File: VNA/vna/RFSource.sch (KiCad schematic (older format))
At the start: 0 parts

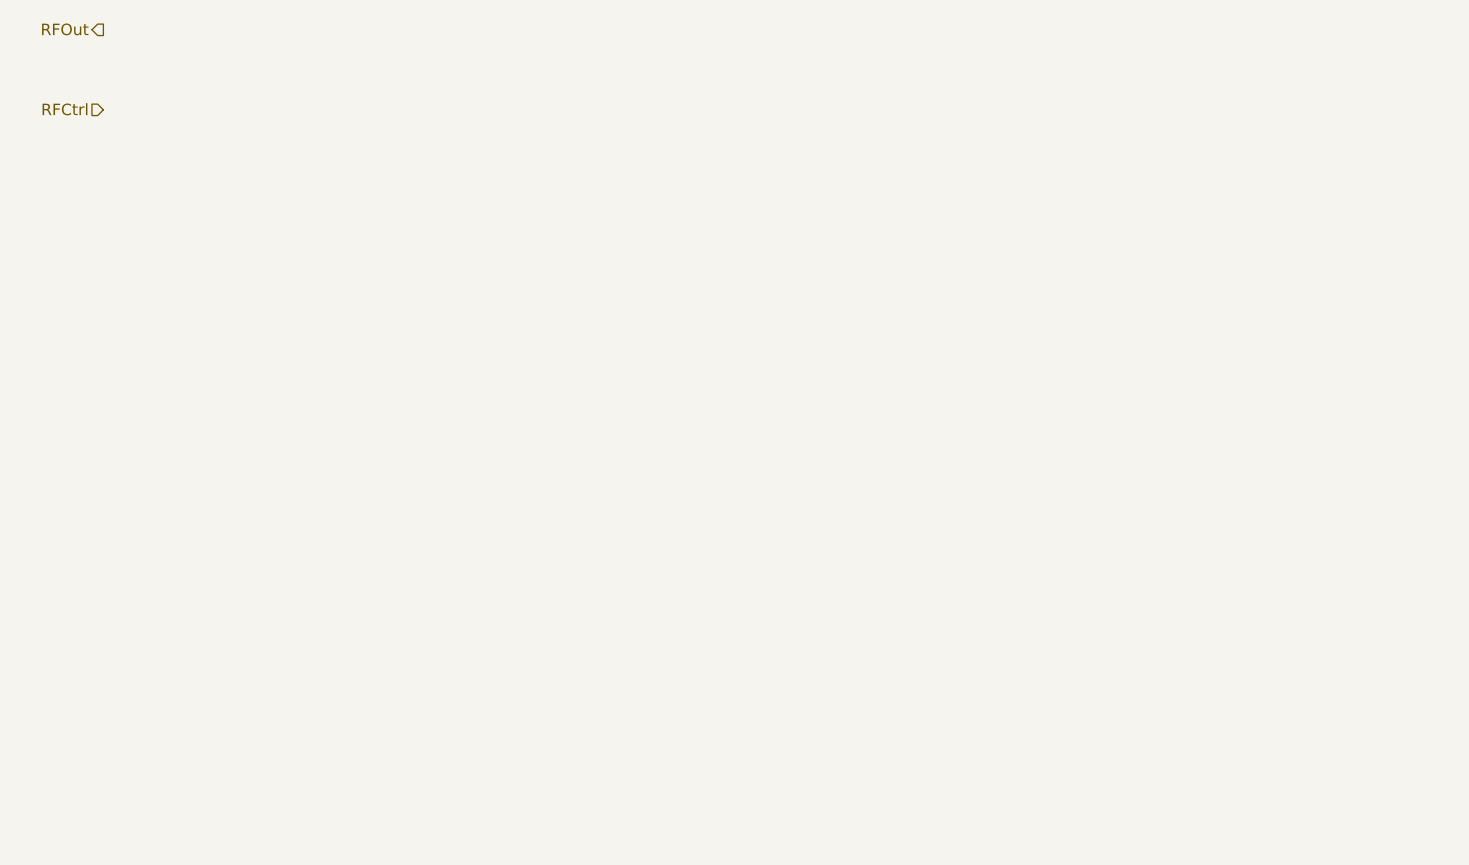
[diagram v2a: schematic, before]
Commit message: finished controller, chose compatible switches
controller and rf switches have been completed.

ToDo: finish filter design for RF Source, add auto gain control
ToDo: finish directional coupler footprints
ToDo: PCB Layout
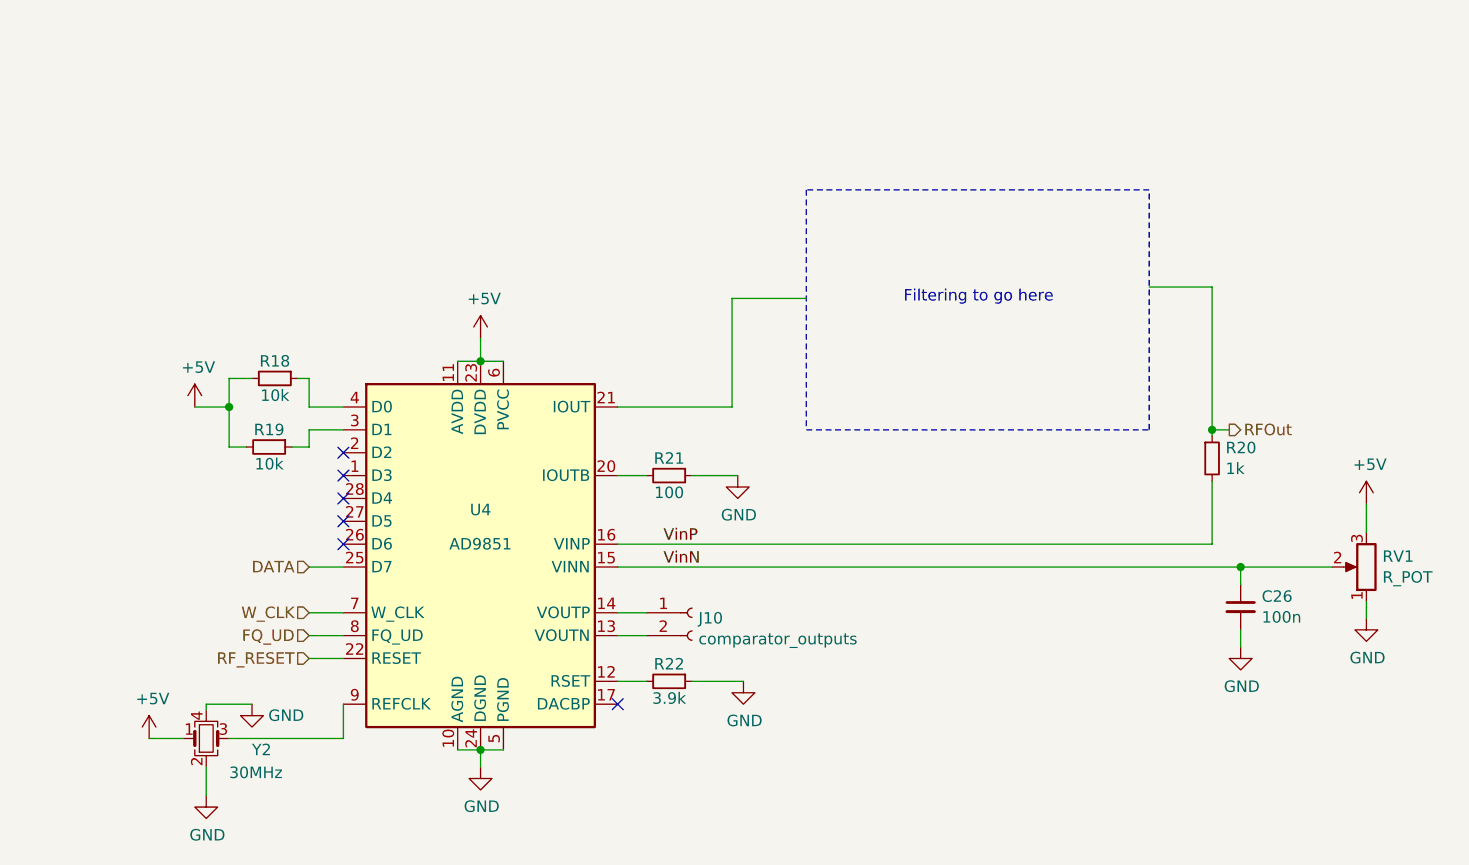
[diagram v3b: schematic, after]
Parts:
- added C26: 100n, symbol Device:C_Small
- added J10: comparator_outputs, symbol Connector:Conn_01x02_Female
- added R18, R19: 10k, symbol Device:R_Small
- added R20: 1k, symbol Device:R_Small
- added R21: 100, symbol Device:R_Small
- added R22: 3.9k, symbol Device:R_Small
- added RV1: R_POT, symbol Device:R_POT
- added U4: AD9851, Package_SO:SSOP-28_5.3x10.2mm_P0.65mm, symbol Interface:AD9851
- added Y2: 30MHz, symbol Device:Crystal_GND24_Small
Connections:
- net labels added: +5V, DATA, FQ_UD, GND, RF_RESET, VinN, VinP, W_CLK
- net labels removed: RFCtrl
- wire segments 0 -> 48
- no-connect marks 0 -> 6
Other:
- note added: "Filtering to go here"

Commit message: custom footprint for couplers, added decoupling caps
added custom footprint for directional couplers - will need to verify it

added decoupling caps to ad9851
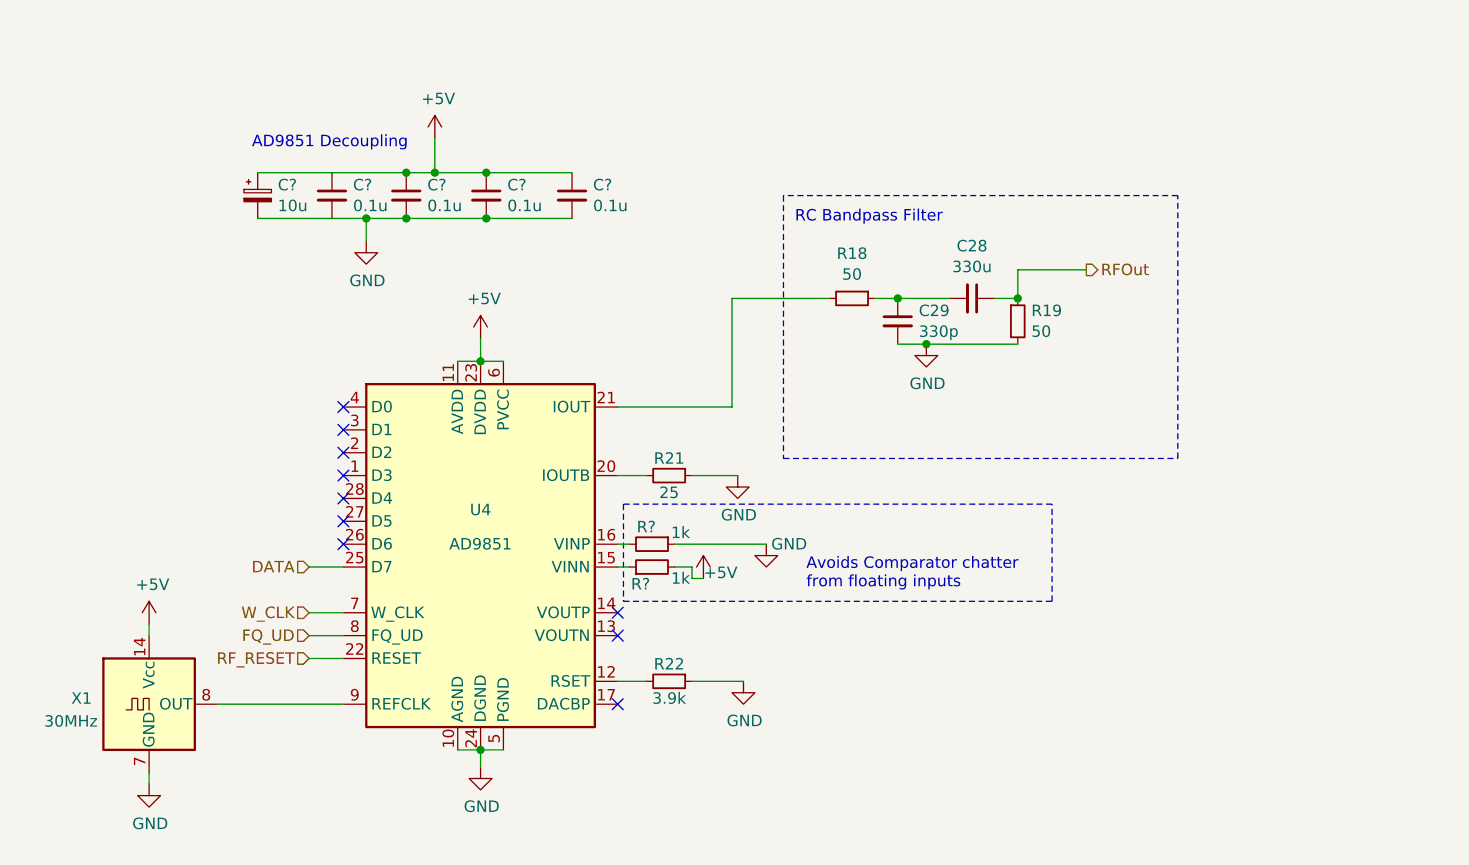
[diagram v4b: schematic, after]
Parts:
- removed C26: 100n, symbol Device:C_Small
- removed J10: comparator_outputs, symbol Connector:Conn_01x02_Female
- removed R20: 1k, symbol Device:R_Small
- removed RV1: R_POT, symbol Device:R_POT
- removed Y2: 30MHz, symbol Device:Crystal_GND24_Small
- added C28: 330u, Capacitor_SMD:C_1206_3216Metric_Pad1.42x1.75mm_HandSolder, symbol Device:C_Small
- added C29: 330p, Capacitor_SMD:C_1206_3216Metric_Pad1.42x1.75mm_HandSolder, symbol Device:C_Small
- added C? (x4): 0.1u, symbol Device:C_Small
- added C?: 10u, symbol Device:CP_Small
- added R? (x2): 1k, symbol Device:R_Small
- added X1: 30MHz, Oscillator:Oscillator_DIP-14, symbol Oscillator:ACO-xxxMHz
- R18, R19: value 10k -> 50; footprint (none) -> Resistor_SMD:R_1206_3216Metric_Pad1.42x1.75mm_HandSolder
- R21: value 100 -> 25; footprint (none) -> Resistor_SMD:R_1206_3216Metric_Pad1.42x1.75mm_HandSolder
- R22: footprint (none) -> Resistor_SMD:R_1206_3216Metric_Pad1.42x1.75mm_HandSolder
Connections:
- net labels removed: VinN, VinP
- wire segments 48 -> 45
- no-connect marks 6 -> 10
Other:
- note added: "AD9851 Decoupling"
- note added: "Avoids Comparator chatter \nfrom floating inputs"
- note added: "RC Bandpass Filter"
- note removed: "Filtering to go here"

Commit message: beginning pcb layout
pcb layout process begun
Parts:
- C31: renamed from C?; footprint (none) -> Capacitor_SMD:CP_Elec_6.3x5.4_Nichicon
- C32, C33, C34, C35: renamed from C?; footprint (none) -> Capacitor_SMD:C_1206_3216Metric_Pad1.42x1.75mm_HandSolder
- R20, R23: renamed from R?; footprint (none) -> Resistor_SMD:R_1206_3216Metric_Pad1.42x1.75mm_HandSolder
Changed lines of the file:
@@
 	7300 3075 5575 3075
 $Comp
-L Device:R_Small R?
+L Device:R_Small R20
 U 1 1 5D955DB5
 P 5000 4600
-F 0 "R?" V 4925 4575 50  0000 C CNN
+F 0 "R20" V 4925 4575 50  0000 C CNN
 F 1 "1k" V 4950 4725 50  0000 C CNN
-F 2 "" H 5000 4600 50  0001 C CNN
+F 2 "Resistor_SMD:R_1206_3216Metric_Pad1.42x1.75mm_HandSolder" H 5000 4600 50  0001 C CNN
 F 3 "~" H 5000 4600 50  0001 C CNN
 	1    5000 4600
@@
 $EndComp
 $Comp
-L Device:R_Small R?
+L Device:R_Small R23
 U 1 1 5D956A76
 P 5000 4700
-F 0 "R?" V 4925 4750 50  0000 C CNN
+F 0 "R23" V 4925 4750 50  0000 C CNN
 F 1 "1k" V 4950 4575 50  0000 C CNN
-F 2 "" H 5000 4700 50  0001 C CNN
+F 2 "Resistor_SMD:R_1206_3216Metric_Pad1.42x1.75mm_HandSolder" H 5000 4700 50  0001 C CNN
 F 3 "~" H 5000 4700 50  0001 C CNN
 	1    5000 4700
@@
 	4850 4700 4900 4700
 $Comp
-L power:GND #PWR?
+L power:GND #PWR0113
 U 1 1 5D95B0FC
 P 5500 4600
-F 0 "#PWR?" H 5500 4350 50  0001 C CNN
+F 0 "#PWR0113" H 5500 4350 50  0001 C CNN
 F 1 "GND" H 5600 4600 50  0000 C CNN
 F 2 "" H 5500 4600 50  0001 C CNN
@@
 	5100 4600 5500 4600
 $Comp
-L power:+5V #PWR?
+L power:+5V #PWR0114
 U 1 1 5D95C83A
 P 5225 4750
-F 0 "#PWR?" H 5225 4600 50  0001 C CNN
+F 0 "#PWR0114" H 5225 4600 50  0001 C CNN
 F 1 "+5V" H 5300 4775 50  0000 C CNN
 F 2 "" H 5225 4750 50  0001 C CNN
@@
 	5175 4750 5225 4750
 $Comp
-L Device:C_Small C?
+L Device:C_Small C35
 U 1 1 5D95F03A
 P 4650 3075
-F 0 "C?" H 4742 3121 50  0000 L CNN
+F 0 "C35" H 4742 3121 50  0000 L CNN
 F 1 "0.1u" H 4742 3030 50  0000 L CNN
-F 2 "" H 4650 3075 50  0001 C CNN
+F 2 "Capacitor_SMD:C_1206_3216Metric_Pad1.42x1.75mm_HandSolder" H 4650 3075 50  0001 C CNN
 F 3 "~" H 4650 3075 50  0001 C CNN
 	1    4650 3075
@@
 $EndComp
 $Comp
-L Device:C_Small C?
+L Device:C_Small C34
 U 1 1 5D961801
 P 4275 3075
-F 0 "C?" H 4367 3121 50  0000 L CNN
+F 0 "C34" H 4367 3121 50  0000 L CNN
 F 1 "0.1u" H 4367 3030 50  0000 L CNN
-F 2 "" H 4275 3075 50  0001 C CNN
+F 2 "Capacitor_SMD:C_1206_3216Metric_Pad1.42x1.75mm_HandSolder" H 4275 3075 50  0001 C CNN
 F 3 "~" H 4275 3075 50  0001 C CNN
 	1    4275 3075
@@
 $EndComp
 $Comp
-L Device:C_Small C?
+L Device:C_Small C33
 U 1 1 5D961E48
 P 3925 3075
-F 0 "C?" H 4017 3121 50  0000 L CNN
+F 0 "C33" H 4017 3121 50  0000 L CNN
 F 1 "0.1u" H 4017 3030 50  0000 L CNN
-F 2 "" H 3925 3075 50  0001 C CNN
+F 2 "Capacitor_SMD:C_1206_3216Metric_Pad1.42x1.75mm_HandSolder" H 3925 3075 50  0001 C CNN
 F 3 "~" H 3925 3075 50  0001 C CNN
 	1    3925 3075
@@
 $EndComp
 $Comp
-L Device:C_Small C?
+L Device:C_Small C32
 U 1 1 5D9624FC
 P 3600 3075
-F 0 "C?" H 3692 3121 50  0000 L CNN
+F 0 "C32" H 3692 3121 50  0000 L CNN
 F 1 "0.1u" H 3692 3030 50  0000 L CNN
-F 2 "" H 3600 3075 50  0001 C CNN
+F 2 "Capacitor_SMD:C_1206_3216Metric_Pad1.42x1.75mm_HandSolder" H 3600 3075 50  0001 C CNN
 F 3 "~" H 3600 3075 50  0001 C CNN
 	1    3600 3075
@@
 Connection ~ 3925 3175
 $Comp
-L Device:CP_Small C?
+L Device:CP_Small C31
 U 1 1 5D9681A5
 P 3275 3075
-F 0 "C?" H 3363 3121 50  0000 L CNN
+F 0 "C31" H 3363 3121 50  0000 L CNN
 F 1 "10u" H 3363 3030 50  0000 L CNN
-F 2 "" H 3275 3075 50  0001 C CNN
+F 2 "Capacitor_SMD:CP_Elec_6.3x5.4_Nichicon" H 3275 3075 50  0001 C CNN
 F 3 "~" H 3275 3075 50  0001 C CNN
 	1    3275 3075
@@
 	3600 3175 3275 3175
 $Comp
-L power:+5V #PWR?
+L power:+5V #PWR0115
 U 1 1 5D968DE4
 P 4050 2825
-F 0 "#PWR?" H 4050 2675 50  0001 C CNN
+F 0 "#PWR0115" H 4050 2675 50  0001 C CNN
 F 1 "+5V" H 4065 2998 50  0000 C CNN
 F 2 "" H 4050 2825 50  0001 C CNN
@@
 $EndComp
 $Comp
-L power:GND #PWR?
+L power:GND #PWR0116
 U 1 1 5D969BB8
 P 3750 3275
-F 0 "#PWR?" H 3750 3025 50  0001 C CNN
+F 0 "#PWR0116" H 3750 3025 50  0001 C CNN
 F 1 "GND" H 3755 3102 50  0000 C CNN
 F 2 "" H 3750 3275 50  0001 C CNN
